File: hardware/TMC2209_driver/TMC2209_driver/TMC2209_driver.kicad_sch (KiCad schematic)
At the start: 21 parts, among them J1 Conn_01x08, J2 Conn_01x08, J3 Conn_01x02

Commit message: finished driver board design
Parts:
- removed C8: 10µF, Capacitor_SMD:C_1206_3216Metric, symbol Device:C
- C1, C2, C3, C4, C5, C9: footprint Capacitor_SMD:C_0603_1608Metric -> Capacitor_SMD:C_0402_1005Metric
- JP1: footprint Jumper:SolderJumper-3_P1.3mm_Open_Pad1.0x1.5mm -> FlexPrint:SolderJumper_3Pads
- R1, R2, R6: footprint Resistor_SMD:R_0603_1608Metric -> Resistor_SMD:R_0402_1005Metric
- R4, R5: footprint Resistor_SMD:R_1206_3216Metric -> Resistor_SMD:R_0805_2012Metric
- RV1: footprint Potentiometer_SMD:Potentiometer_Bourns_3314J_Vertical -> FlexPrint:TRIMMER_3312J-1-203E
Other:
- moved on the sheet: C6, C7
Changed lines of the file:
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@@
 	(wire
 		(pts
-			(xy 63.5 97.79) (xy 66.04 97.79)
+			(xy 115.57 55.88) (xy 124.46 55.88)
 		)
 		(stroke
@@
 	(wire
 		(pts
-			(xy 179.07 119.38) (xy 186.69 119.38)
+			(xy 63.5 97.79) (xy 66.04 97.79)
 		)
 		(stroke
@@
 	(wire
 		(pts
-			(xy 63.5 66.04) (xy 66.04 66.04)
+			(xy 179.07 119.38) (xy 186.69 119.38)
 		)
 		(stroke
@@
 	(wire
 		(pts
-			(xy 114.3 55.88) (xy 124.46 55.88)
+			(xy 63.5 66.04) (xy 66.04 66.04)
 		)
 		(stroke
@@
 	(wire
 		(pts
-			(xy 114.3 48.26) (xy 124.46 48.26)
-		)
-		(stroke
-			(width 0)
-			(type default)
-		)
-	)
-	(wire
-		(pts
 			(xy 116.84 124.46) (xy 116.84 127)
 		)
@@
 	(wire
 		(pts
-			(xy 124.46 55.88) (xy 134.62 55.88)
+			(xy 124.46 55.88) (xy 133.35 55.88)
 		)
 		(stroke
@@
 	(wire
 		(pts
-			(xy 124.46 48.26) (xy 134.62 48.26)
+			(xy 124.46 48.26) (xy 133.35 48.26)
 		)
 		(stroke
@@
 	(wire
 		(pts
+			(xy 115.57 48.26) (xy 124.46 48.26)
+		)
+		(stroke
+			(width 0)
+			(type default)
+		)
+	)
+	(wire
+		(pts
 			(xy 142.24 99.06) (xy 146.05 99.06)
 		)
@@
 	(symbol
 		(lib_id "Device:C")
-		(at 124.46 52.07 0)
+		(at 115.57 52.07 0)
 		(unit 1)
 		(exclude_from_sim no)
@@
 		(dnp no)
 		(property "Reference" "C7"
-			(at 126.746 51.054 0)
+			(at 117.856 51.054 0)
 			(effects
 				(font
@@
 		)
 		(property "Value" "10µF"
-			(at 126.746 53.594 0)
+			(at 117.856 53.594 0)
 			(effects
 				(font
@@
 		)
 		(property "Footprint" "Capacitor_SMD:C_1206_3216Metric"
-			(at 125.4252 55.88 0)
+			(at 116.5352 55.88 0)
 			(effects
 				(font
@@
 		)
 		(property "Datasheet" "~"
-			(at 124.46 52.07 0)
+			(at 115.57 52.07 0)
 			(effects
 				(font
@@
 		)
 		(property "Description" "Unpolarized capacitor"
-			(at 124.46 52.07 0)
+			(at 115.57 52.07 0)
 			(effects
 				(font
@@
 			)
 		)
-		(property "Footprint" "Capacitor_SMD:C_0603_1608Metric"
+		(property "Footprint" "Capacitor_SMD:C_0402_1005Metric"
 			(at 187.6552 106.68 0)
 			(effects
@@
 			)
 		)
-		(property "Footprint" "Resistor_SMD:R_1206_3216Metric"
+		(property "Footprint" "Resistor_SMD:R_0805_2012Metric"
 			(at 192.532 123.19 90)
 			(effects
@@
 			)
 		)
-		(property "Footprint" "Resistor_SMD:R_0603_1608Metric"
+		(property "Footprint" "Resistor_SMD:R_0402_1005Metric"
 			(at 110.49 109.982 90)
 			(effects
@@
 			)
 		)
-		(property "Footprint" "Capacitor_SMD:C_0603_1608Metric"
+		(property "Footprint" "Capacitor_SMD:C_0402_1005Metric"
 			(at 143.51 73.9648 0)
 			(effects
@@
 			)
 		)
-		(property "Footprint" "Capacitor_SMD:C_0603_1608Metric"
+		(property "Footprint" "Capacitor_SMD:C_0402_1005Metric"
 			(at 160.9852 55.88 0)
 			(effects
@@
 			)
 		)
-		(property "Footprint" "Capacitor_SMD:C_0603_1608Metric"
+		(property "Footprint" "Capacitor_SMD:C_0402_1005Metric"
 			(at 195.2752 106.68 0)
 			(effects
@@
 			)
 		)
-		(property "Footprint" "Resistor_SMD:R_0603_1608Metric"
+		(property "Footprint" "Resistor_SMD:R_0402_1005Metric"
 			(at 127.762 120.65 90)
 			(effects
@@
 	)
 	(symbol
-		(lib_id "Device:C")
-		(at 114.3 52.07 0)
-		(unit 1)
-		(exclude_from_sim no)
-		(in_bom yes)
-		(on_board yes)
-		(dnp no)
-		(property "Reference" "C8"
-			(at 116.586 50.8 0)
-			(effects
-				(font
-					(size 1.27 1.27)
-				)
-				(justify left)
-			)
-		)
-		(property "Value" "10µF"
-			(at 116.586 53.34 0)
-			(effects
-				(font
-					(size 1.27 1.27)
-				)
-				(justify left)
-			)
-		)
-		(property "Footprint" "Capacitor_SMD:C_1206_3216Metric"
-			(at 115.2652 55.88 0)
-			(effects
-				(font
-					(size 1.27 1.27)
-				)
-				(hide yes)
-			)
-		)
-		(property "Datasheet" "~"
-			(at 114.3 52.07 0)
-			(effects
-				(font
-					(size 1.27 1.27)
-				)
-				(hide yes)
-			)
-		)
-		(property "Description" "Unpolarized capacitor"
-			(at 114.3 52.07 0)
-			(effects
-				(font
-					(size 1.27 1.27)
-				)
-				(hide yes)
-			)
-		)
-		(pin "1"
-		)
-		(pin "2"
-		)
-		(instances
-			(project ""
-				(path "/ffb67535-1c6e-42d2-9b3b-d74a0518d54b"
-					(reference "C8")
-					(unit 1)
-				)
-			)
-		)
-	)
-	(symbol
 		(lib_id "power:GND")
 		(at 186.69 129.54 0)
@@
 			)
 		)
-		(property "Footprint" "Capacitor_SMD:C_0603_1608Metric"
+		(property "Footprint" "Capacitor_SMD:C_0402_1005Metric"
 			(at 168.6052 67.31 0)
 			(effects
@@
 			)
 		)
-		(property "Footprint" "Resistor_SMD:R_0603_1608Metric"
+		(property "Footprint" "Resistor_SMD:R_0402_1005Metric"
 			(at 123.952 82.55 90)
 			(effects
@@
 			)
 		)
-		(property "Footprint" "Jumper:SolderJumper-3_P1.3mm_Open_Pad1.0x1.5mm"
+		(property "Footprint" "FlexPrint:SolderJumper_3Pads"
 			(at 83.82 58.42 0)
 			(effects
@@
 			)
 		)
-		(property "Footprint" "Potentiometer_SMD:Potentiometer_Bourns_3314J_Vertical"
+		(property "Footprint" "FlexPrint:TRIMMER_3312J-1-203E"
 			(at 116.84 120.65 0)
 			(effects
@@
 			)
 		)
-		(property "Footprint" "Resistor_SMD:R_1206_3216Metric"
+		(property "Footprint" "Resistor_SMD:R_0805_2012Metric"
 			(at 184.912 123.19 90)
 			(effects
@@
 			)
 		)
-		(property "Footprint" "Capacitor_SMD:C_0603_1608Metric"
+		(property "Footprint" "Capacitor_SMD:C_0402_1005Metric"
 			(at 149.5552 55.88 0)
 			(effects
@@
 	(symbol
 		(lib_id "Device:C")
-		(at 134.62 52.07 0)
+		(at 133.35 52.07 0)
 		(unit 1)
 		(exclude_from_sim no)
@@
 		(dnp no)
 		(property "Reference" "C6"
-			(at 137.16 50.8 0)
+			(at 135.89 50.8 0)
 			(effects
 				(font
@@
 		)
 		(property "Value" "10µF"
-			(at 137.16 53.34 0)
+			(at 135.89 53.34 0)
 			(effects
 				(font
@@
 		)
 		(property "Footprint" "Capacitor_SMD:C_1206_3216Metric"
-			(at 135.5852 55.88 0)
+			(at 134.3152 55.88 0)
 			(effects
 				(font
@@
 		)
 		(property "Datasheet" "~"
-			(at 134.62 52.07 0)
+			(at 133.35 52.07 0)
 			(effects
 				(font
@@
 		)
 		(property "Description" "Unpolarized capacitor"
-			(at 134.62 52.07 0)
+			(at 133.35 52.07 0)
 			(effects
 				(font

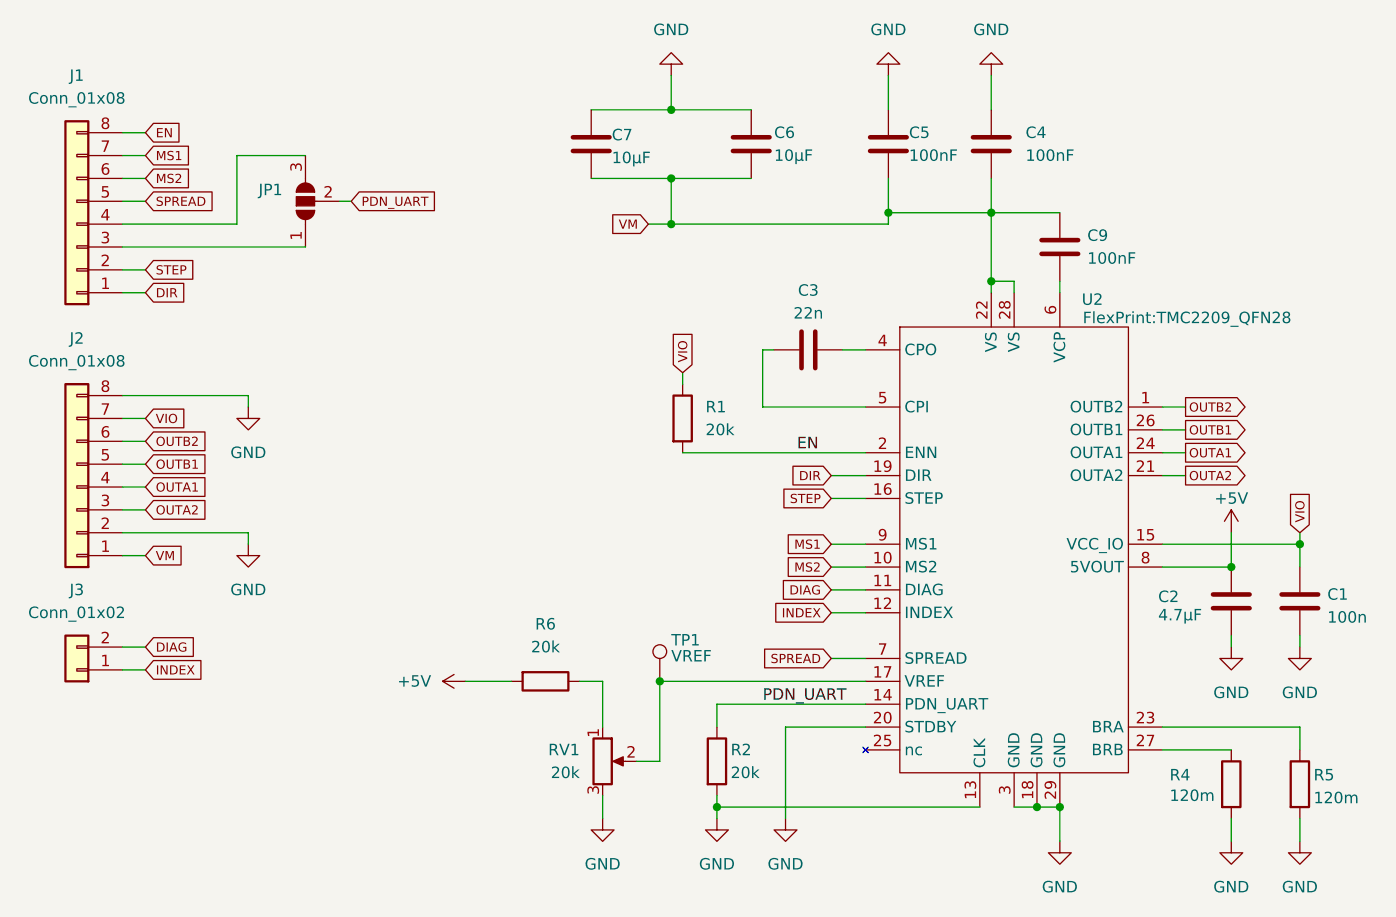
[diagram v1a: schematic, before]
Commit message: Mainboard-3
Version 3 of Mainboard, (version 2 not uploaded)
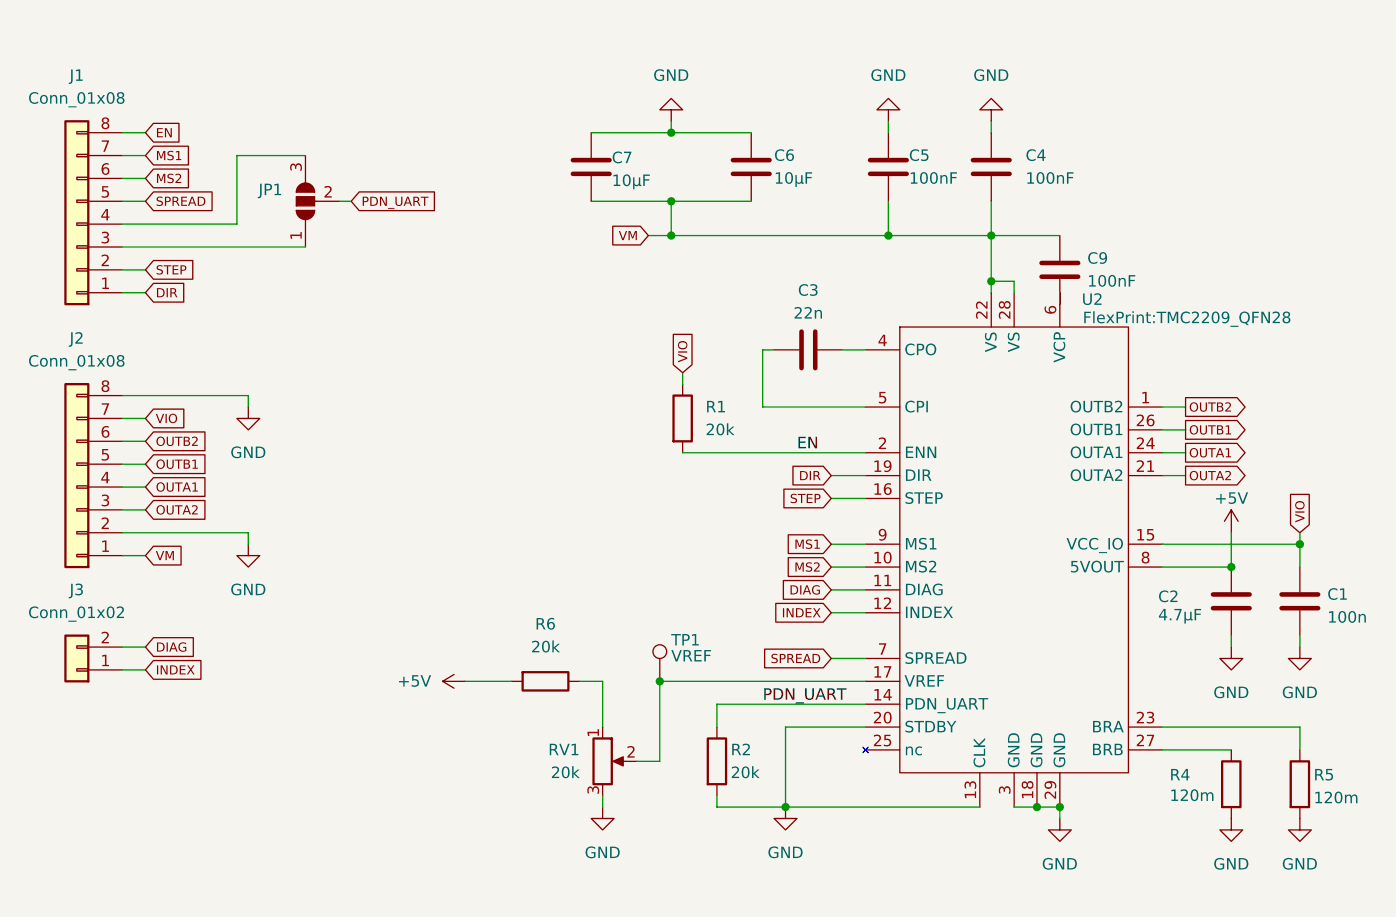
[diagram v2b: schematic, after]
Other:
- moved on the sheet: C4, C5, C6, C7, C9
